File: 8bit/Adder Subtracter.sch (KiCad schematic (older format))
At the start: 0 parts

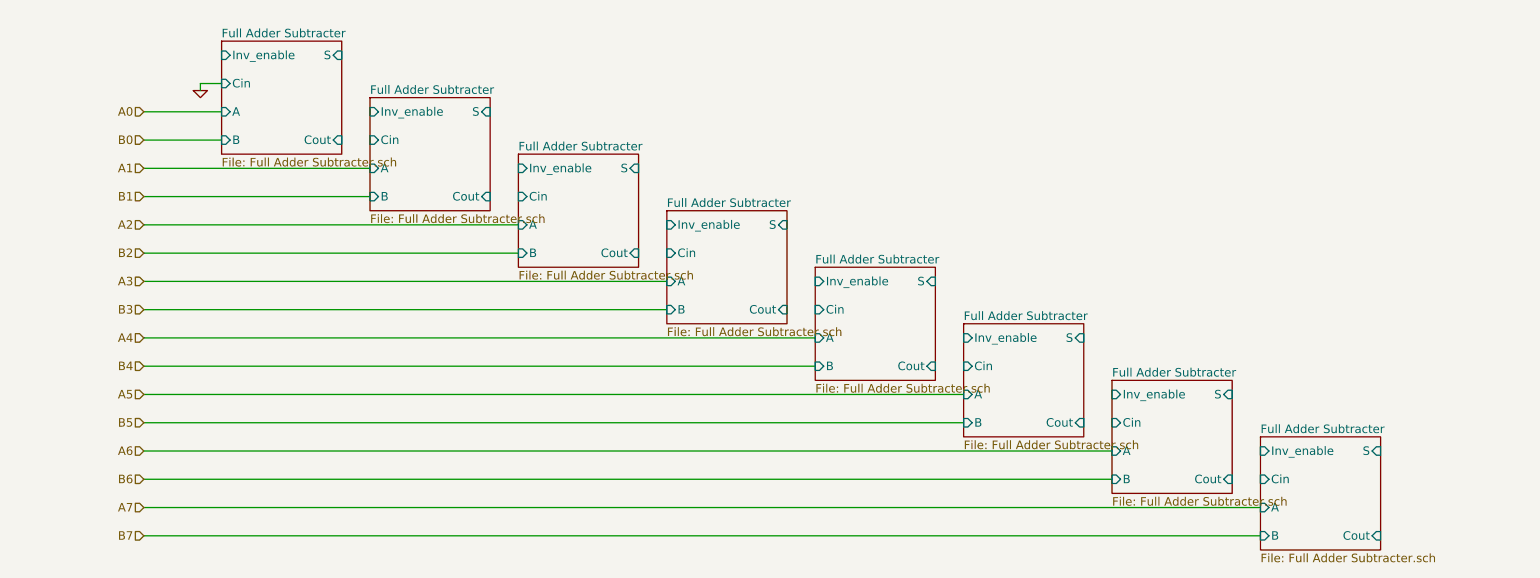
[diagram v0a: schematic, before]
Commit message: Added top level hierarchical diagram
Created 1-bit counter
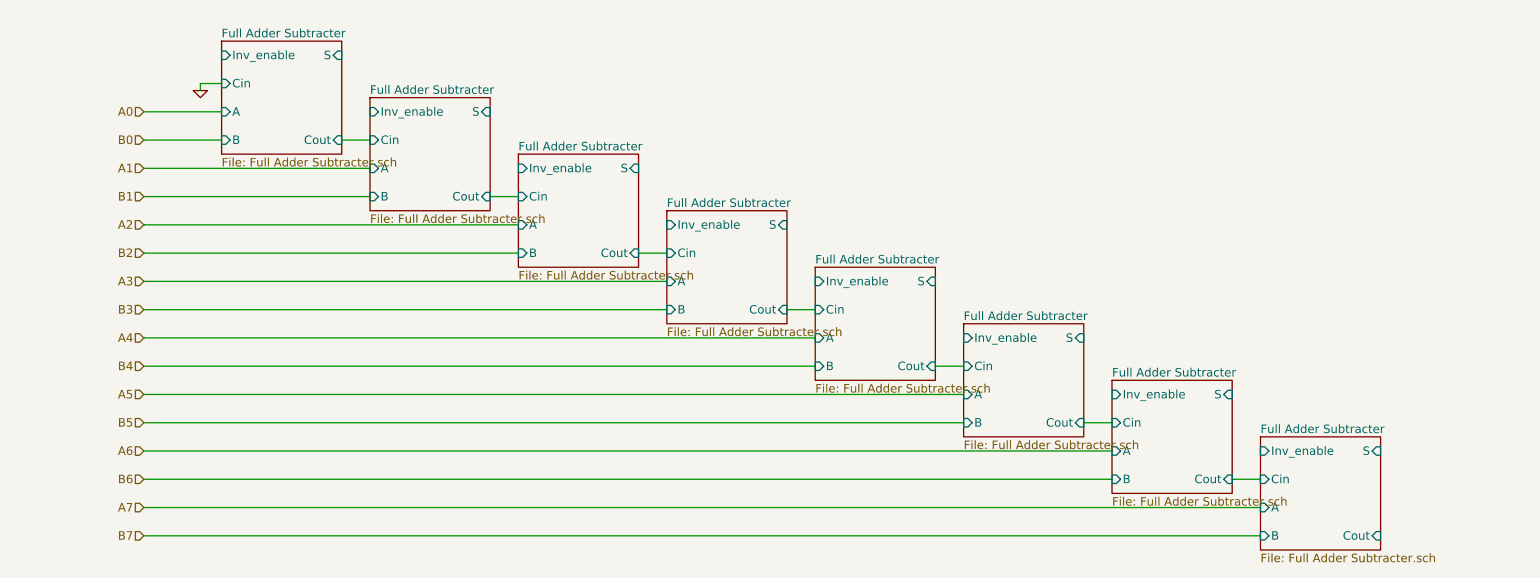
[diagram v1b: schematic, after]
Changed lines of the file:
@@
 $Descr A4 11693 8268
 encoding utf-8
-Sheet 3 11
+Sheet 3 27
 Title ""
 Date ""
@@
 Wire Wire Line
 	9300 5350 1400 5350
+Wire Wire Line
+	2800 2550 3000 2550
+Wire Wire Line
+	3850 2950 4050 2950
+Wire Wire Line
+	4900 3350 5100 3350
+Wire Wire Line
+	5950 3750 6150 3750
+Wire Wire Line
+	7000 4150 7200 4150
+Wire Wire Line
+	8050 4550 8250 4550
+Wire Wire Line
+	9100 4950 9300 4950
 $EndSCHEMATC

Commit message: Created 16:8 mux sheet for simplicity
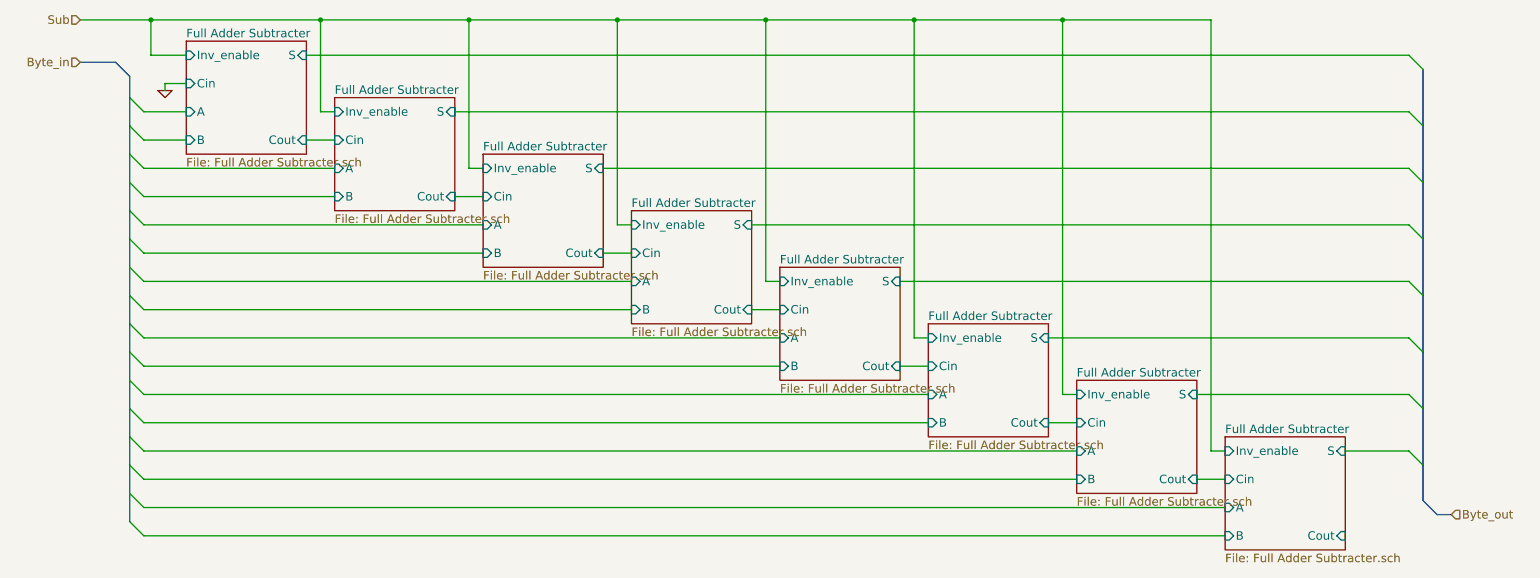
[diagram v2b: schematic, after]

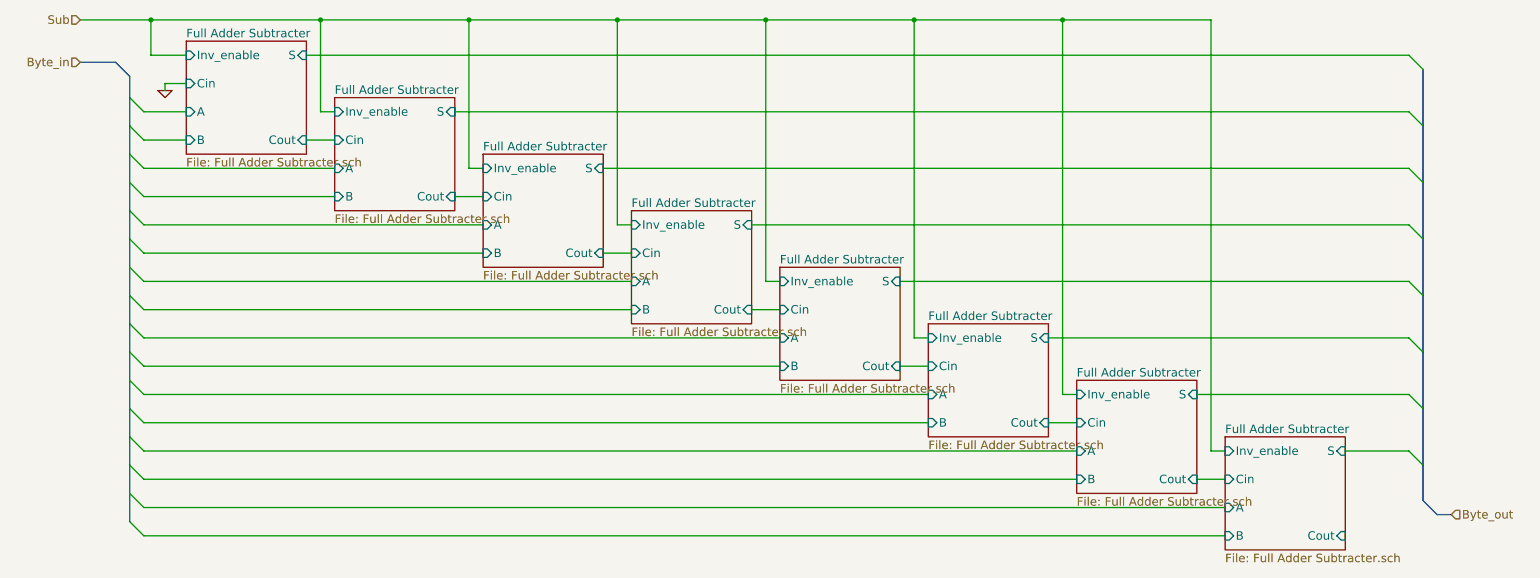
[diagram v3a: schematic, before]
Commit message: Added Comparator to ALU, removed NAND
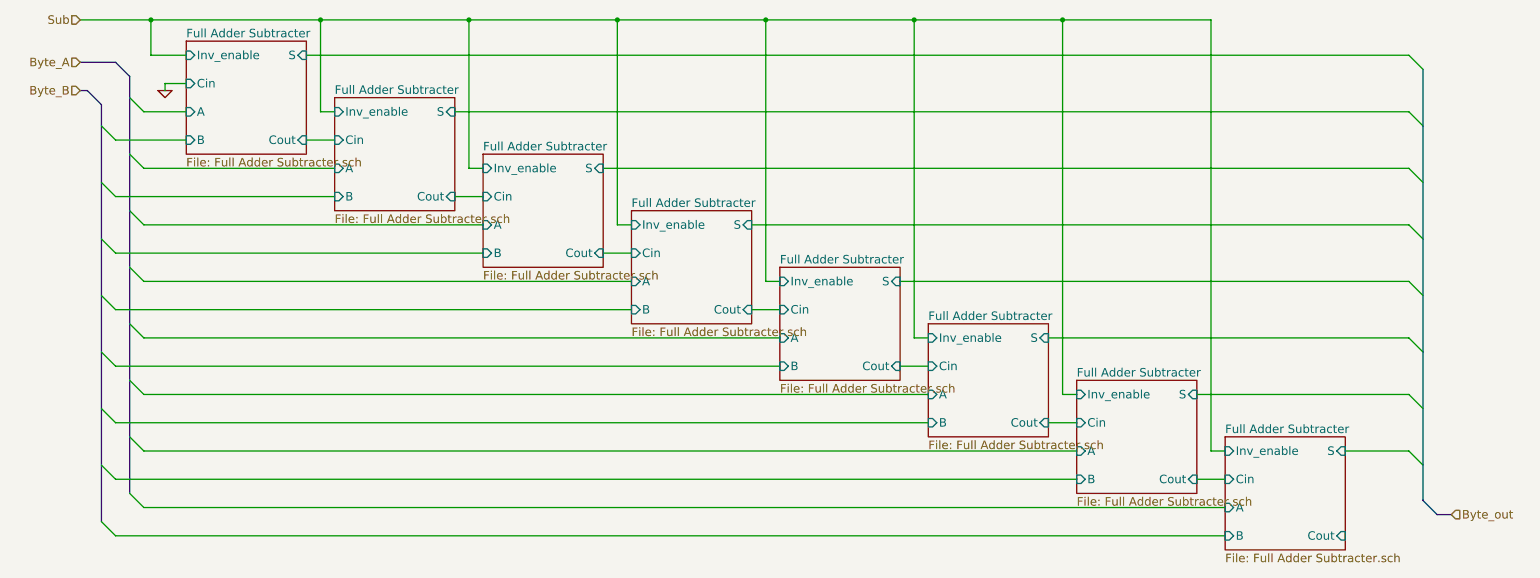
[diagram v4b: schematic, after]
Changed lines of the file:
@@
 $Descr A4 11693 8268
 encoding utf-8
-Sheet 3 29
+Sheet 3 28
 Title ""
 Date ""
@@
 	1400 2350 1700 2350
 Wire Wire Line
-	1400 2550 1700 2550
+	1200 2550 1700 2550
 $Sheet
 S 2750 2250 850  800
@@
 	1400 2750 2750 2750
 Wire Wire Line
-	1400 2950 2750 2950
+	1200 2950 2750 2950
 Wire Wire Line
 	1400 3150 3800 3150
 Wire Wire Line
-	3800 3350 1400 3350
+	3800 3350 1200 3350
 Wire Wire Line
 	1400 3550 4850 3550
 Wire Wire Line
-	4850 3750 1400 3750
+	4850 3750 1200 3750
 Wire Wire Line
 	1400 3950 5900 3950
 Wire Wire Line
-	5900 4150 1400 4150
+	5900 4150 1200 4150
 Wire Wire Line
 	1400 4350 6950 4350
 Wire Wire Line
-	6950 4550 1400 4550
+	6950 4550 1200 4550
 Wire Wire Line
 	1400 4750 8000 4750
 Wire Wire Line
-	8000 4950 1400 4950
+	8000 4950 1200 4950
 Wire Wire Line
 	1400 5150 9050 5150
 Wire Wire Line
-	9050 5350 1400 5350
+	9050 5350 1200 5350
 Wire Wire Line
 	2550 2550 2750 2550
@@
 	1300 2250 1400 2350
 Entry Wire Line
-	1300 2450 1400 2550
+	1100 2450 1200 2550
 Entry Wire Line
 	1300 2650 1400 2750
 Entry Wire Line
-	1300 2850 1400 2950
+	1100 2850 1200 2950
 Entry Wire Line
 	1300 3050 1400 3150
 Entry Wire Line
-	1300 3250 1400 3350
+	1100 3250 1200 3350
 Entry Wire Line
 	1300 3450 1400 3550
 Entry Wire Line
-	1300 3650 1400 3750
+	1100 3650 1200 3750
 Entry Wire Line
 	1300 3850 1400 3950
 Entry Wire Line
-	1300 4050 1400 4150
+	1100 4050 1200 4150
 Entry Wire Line
 	1300 4250 1400 4350
 Entry Wire Line
-	1300 4450 1400 4550
+	1100 4450 1200 4550
 Entry Wire Line
 	1300 4650 1400 4750
 Entry Wire Line
-	1300 4850 1400 4950
+	1100 4850 1200 4950
 Entry Wire Line
 	1300 5050 1400 5150
 Entry Wire Line
-	1300 5250 1400 5350
-Wire Bus Line
-	1300 2100 1300 2250
-Wire Bus Line
-	1300 2250 1300 2450
-Wire Bus Line
-	1300 2450 1300 2650
-Wire Bus Line
-	1300 2650 1300 2850
-Wire Bus Line
-	1300 2850 1300 3050
-Wire Bus Line
-	1300 3050 1300 3250
-Wire Bus Line
-	1300 3250 1300 3450
-Wire Bus Line
-	1300 3450 1300 3650
-Wire Bus Line
-	1300 3650 1300 3850
-Wire Bus Line
-	1300 3850 1300 4050
-Wire Bus Line
-	1300 4050 1300 4250
-Wire Bus Line
-	1300 4250 1300 4450
-Wire Bus Line
-	1300 4450 1300 4650
-Wire Bus Line
-	1300 4650 1300 4850
-Wire Bus Line
-	1300 4850 1300 5050
-Wire Bus Line
-	1300 5050 1300 5250
+	1100 5250 1200 5350
+Wire Bus Line
+	1300 2100 1300 5050
 Wire Bus Line
 	1300 2100 1200 2000
@@
 	1200 2000 950  2000
 Text HLabel 950  2000 0    60   Input ~ 0
-Byte_in
+Byte_A
 Wire Wire Line
 	9900 4750 10350 4750
@@
 	10350 4750 10450 4850
 Wire Bus Line
-	10450 2050 10450 2450
-Wire Bus Line
-	10450 2450 10450 2850
-Wire Bus Line
-	10450 2850 10450 3250
-Wire Bus Line
-	10450 3250 10450 3650
-Wire Bus Line
-	10450 3650 10450 4050
-Wire Bus Line
-	10450 4050 10450 4450
-Wire Bus Line
-	10450 4450 10450 4850
-Wire Bus Line
-	10450 4850 10450 5100
+	10450 2050 10450 5100
 Wire Wire Line
 	2550 1950 10350 1950
@@
 Sub
 Wire Wire Line
-	950  1700 1450 1700
-Wire Wire Line
-	1450 1700 2650 1700
-Wire Wire Line
-	2650 1700 3700 1700
-Wire Wire Line
-	3700 1700 4750 1700
-Wire Wire Line
-	4750 1700 5800 1700
-Wire Wire Line
-	5800 1700 6850 1700
-Wire Wire Line
-	6850 1700 7900 1700
-Wire Wire Line
-	7900 1700 8950 1700
+	950  1700 8950 1700
 Wire Wire Line
 	1450 1700 1450 1950
@@
 	8950 4750 9050 4750
 Connection ~ 7900 1700
+Wire Bus Line
+	1100 2300 1100 5250
+Wire Bus Line
+	1100 2300 1000 2200
+Wire Bus Line
+	1000 2200 950  2200
+Text HLabel 950  2200 0    60   Input ~ 0
+Byte_B
 $EndSCHEMATC
